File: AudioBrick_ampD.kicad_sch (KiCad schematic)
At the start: 5 parts, among them U1 TPA3251

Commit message: add
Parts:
- U1: value TPA3251 -> TPA313xD2

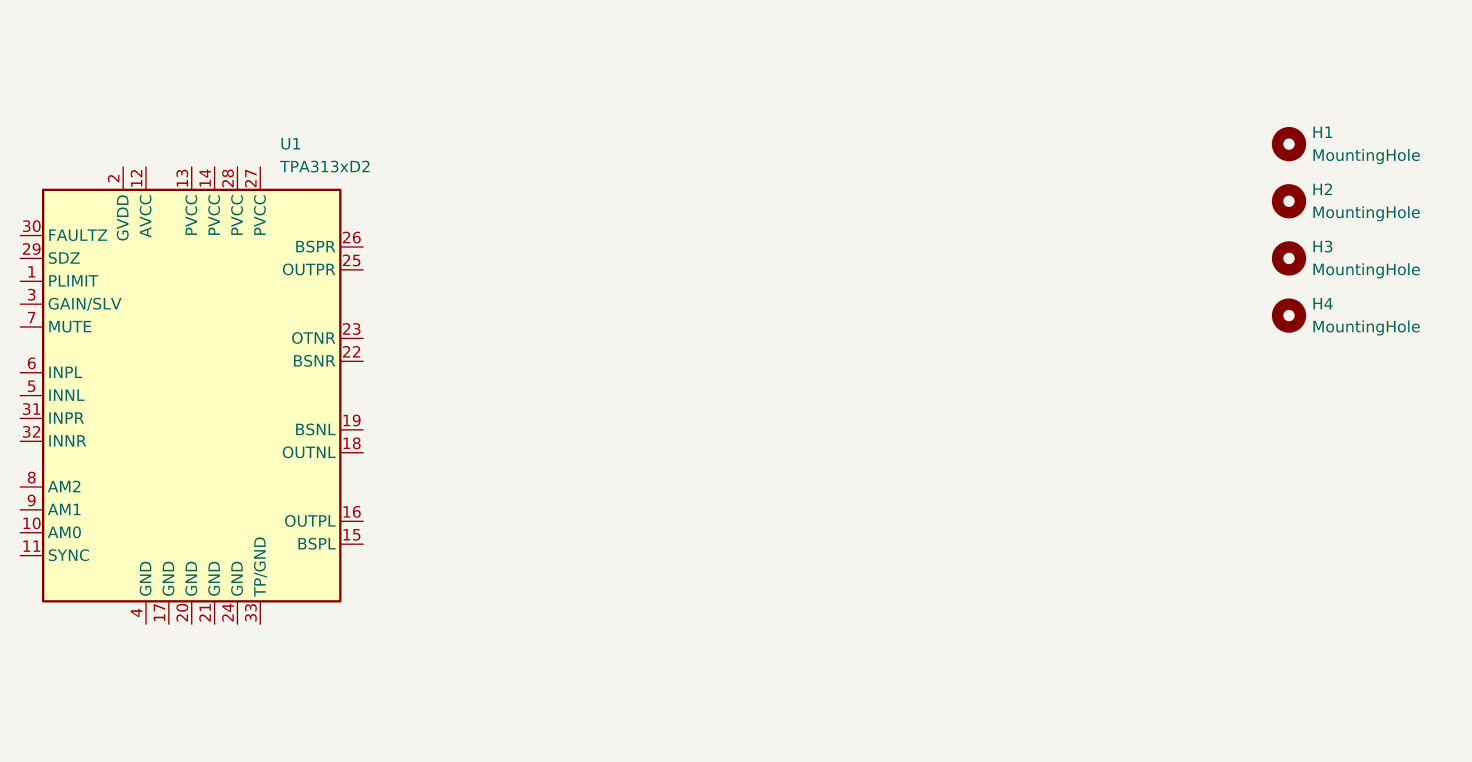
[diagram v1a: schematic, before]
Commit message: output LC filter
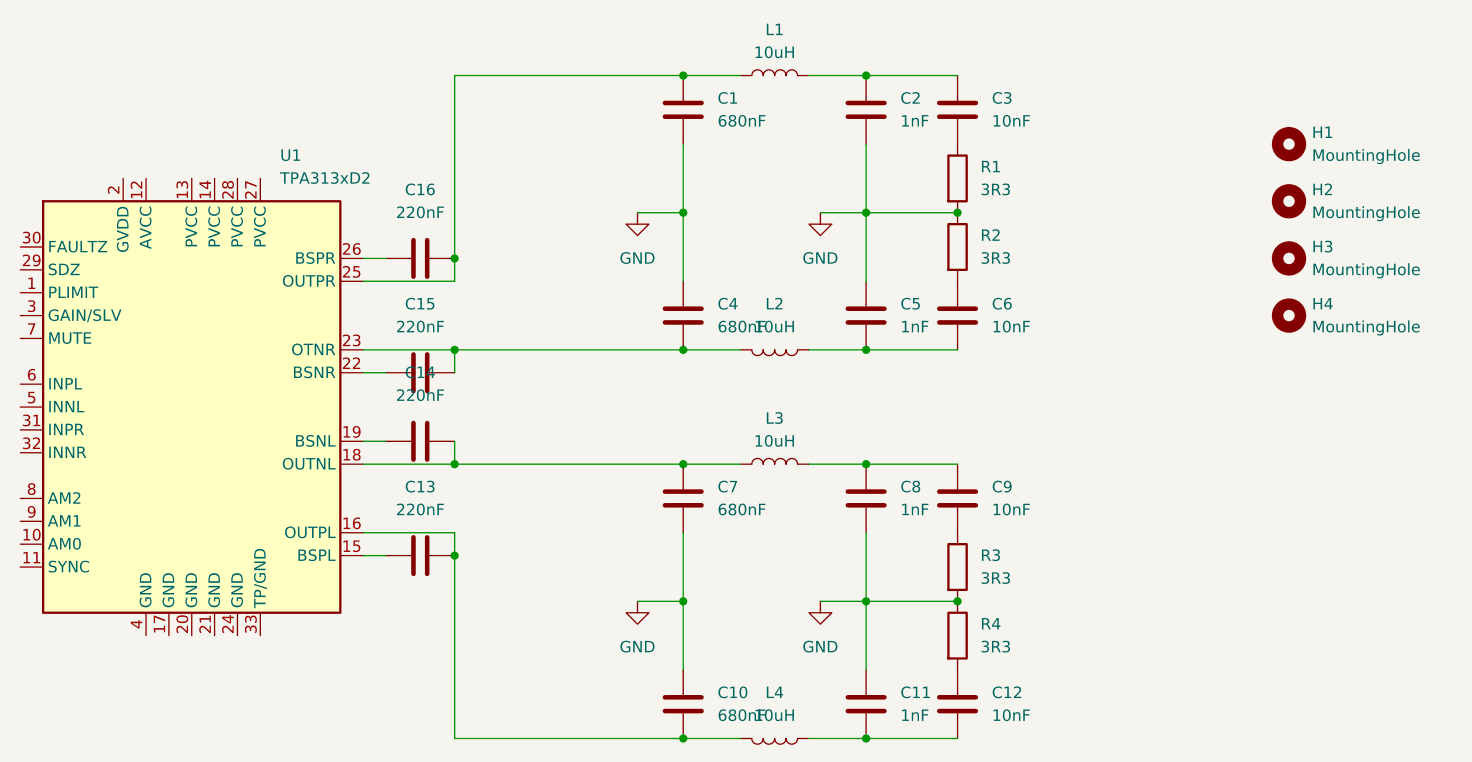
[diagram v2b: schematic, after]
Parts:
- added C1, C10, C4, C7: 680nF, Capacitor_SMD:C_0603_1608Metric, symbol Device:C
- added C11, C2, C5, C8: 1nF, Capacitor_SMD:C_0603_1608Metric, symbol Device:C
- added C12, C3, C6, C9: 10nF, Capacitor_SMD:C_0603_1608Metric, symbol Device:C
- added C13, C14, C15, C16: 220nF, Capacitor_SMD:C_0603_1608Metric, symbol Device:C
- added L1, L2, L3, L4: 10uH, Inductor_SMD:L_10.4x10.4_H4.8, symbol Device:L
- added R1, R2, R3, R4: 3R3, Resistor_SMD:R_0603_1608Metric, symbol Device:R
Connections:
- net at U1.15 (BSPL): now also C13.1
- net at U1.16 (OUTPL): now also C10.2, C13.2, L4.1
- net at U1.18 (OUTNL): now also C14.2, C7.1, L3.2
- net at U1.19 (BSNL): now also C14.1
- net at U1.22 (BSNR): now also C15.1
- net at U1.23 (OTNR): now also C15.2, C4.2, L2.2
- net at U1.25 (OUTPR): now also C1.1, C16.2, L1.1
- net at U1.26 (BSPR): now also C16.1
- new net: C2.1, C3.1, L1.2
- new net: C3.2, R1.1
- new net: C12.1, R4.2
- new net: C8.1, C9.1, L3.1
- new net: C5.2, C6.2, L2.1
- new net: C11.2, C12.2, L4.2
- new net: C6.1, R2.2
- new net: C9.2, R3.1
- new net GND: C1.2, C10.1, C11.1, C2.2, C4.1, C5.1, C7.2, C8.2, R1.2, R2.1, R3.2, R4.1
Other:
- moved on the sheet: U1
